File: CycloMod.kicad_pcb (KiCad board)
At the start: 4 copper layers, 22 x 22 mm, 72 parts, among them J1 MICROMOD-2222, U1 10CL010YM164, U2 W25Q128JVS, U3 1.2V, U4 RP2350_60QFN, U5 MIC5504-2.5YMT, Y1 ABM8-272-T3

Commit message: all connected, cleaning up
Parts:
- C23: moved to B.Cu
- R5, R7: moved to F.Cu
- moved C3 10.6 mm to (149.1, 99.4), turned to 0 degrees
- moved C23 10.4 mm to (157.4, 108.1), turned to -90 degrees
- moved R7 7.80 mm to (149.9, 98.8), turned to -90 degrees
- moved R5 7.35 mm to (148.7, 98.3), turned to 0 degrees
- moved C22 4.32 mm to (158.7, 104.0)
- moved C25 2.55 mm to (152.8, 100.4), turned to 0 degrees
- moved C24 1.41 mm to (153.9, 106.7), turned to 0 degrees
- moved D1 1.00 mm to (142.5, 95.8)
- moved D2 1.00 mm to (145.0, 95.7)
- moved D3 1.00 mm to (147.5, 95.7)
- moved R10 1.00 mm to (143.8, 95.2)
- moved R11 1.00 mm to (146.2, 96.2)
- moved R14 1.00 mm to (146.2, 95.2)
- moved R9 1.00 mm to (143.8, 96.2)
- moved U2 1.00 mm to (145.0, 97.5)
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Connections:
- J1 pad GND: (no net) -> GND
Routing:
- net /~{BOOT}: track 39.2 -> 28.6 mm, vias 1 -> 2
- net +3V3: track 54.4 -> 49.3 mm, vias 20 -> 21
- net /QSPI_SS: track 12.8 -> 10.8 mm
- net /G11: track 17.5 -> 15.6 mm
- net /QSPI_SD2: track 16.0 -> 17.7 mm
- net +2V5: track 34.5 -> 33.3 mm
- net Net-(U1E-VCCD_PLL1): track 29.8 -> 29.2 mm
- net GND: track 71.8 -> 71.7 mm, vias 45 -> 51
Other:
- board text added: "CycloMod"

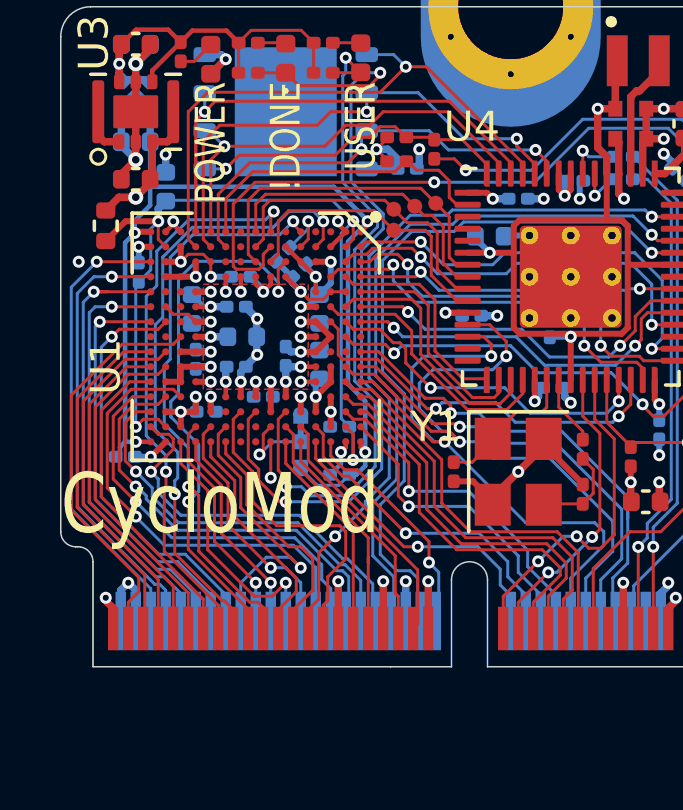
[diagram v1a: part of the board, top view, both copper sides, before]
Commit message: cleaning up nets
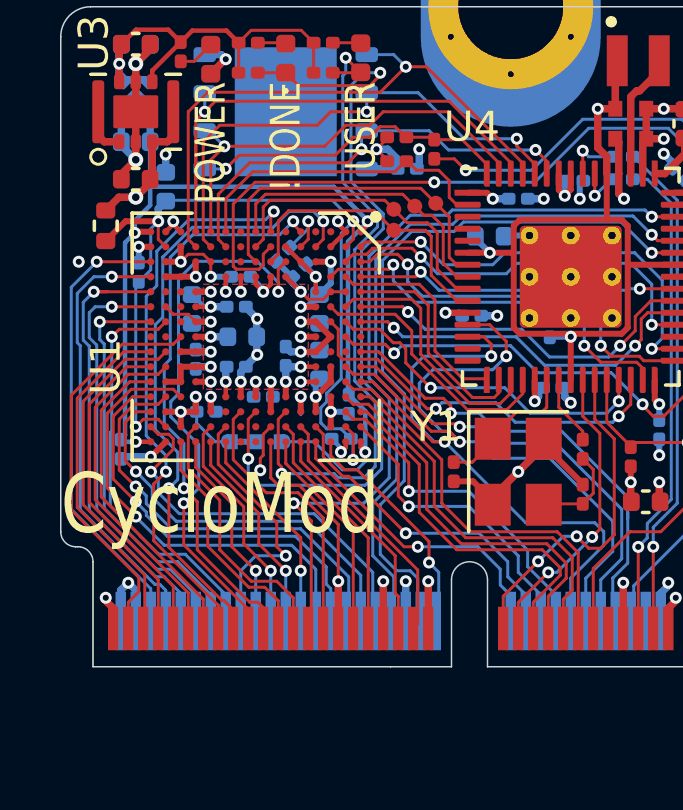
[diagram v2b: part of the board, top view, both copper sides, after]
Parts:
- moved C14 2.37 mm to (147.1, 107.2), turned to -90 degrees
- moved JP2 1.50 mm to (144.0, 108.5), turned to 0 degrees
- moved C30 0.40 mm to (146.8, 108.4)
- moved C15 0.29 mm to (139.5, 108.8), turned to -90 degrees
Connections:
- U1 pad K15: /SDA1 -> /AUD_BCLK
- U1 pad L14: /AUD_BCLK -> /AUD_IN
- U1 pad L15: /SCL1 -> /AUD_LRCLK
- U1 pad M14: /AUD_OUT -> /SDA1
- U1 pad M15: /AUD_IN -> /AUD_OUT
- U1 pad N15: /AUD_LRCLK -> /SCL1
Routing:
- net GND: track 71.7 -> 78.5 mm, vias 51 -> 50
- net /BATT_VIN/3: track 24.7 -> 26.5 mm
- net /AUD_LRCLK: track 8.68 -> 7.01 mm
- net /PWM1: track 10.4 -> 9.19 mm
- net /AUD_BCLK: track 8.22 -> 7.01 mm
- net /MSEL1: track 2.63 -> 1.59 mm
- net /AUD_MCLK: track 9.71 -> 8.72 mm
- net /SDA1: track 7.93 -> 8.78 mm
- net Net-(U1E-VCCD_PLL1): track 29.2 -> 30.0 mm
- net /AUD_OUT: track 7.54 -> 6.80 mm
- net /INIT: track 22.6 -> 21.9 mm
- net /AUD_IN: track 7.01 -> 7.51 mm
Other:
- board text added: "AS|JTAG"
- board text removed: "JT AS"

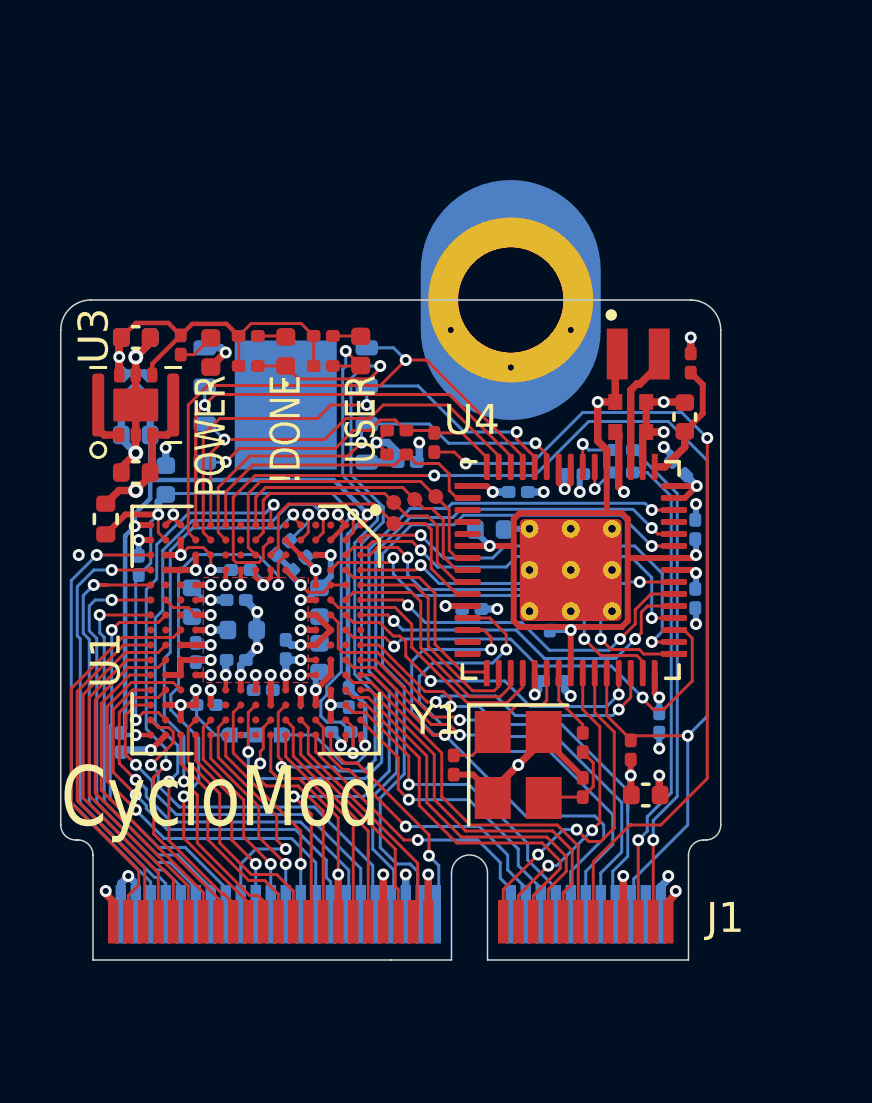
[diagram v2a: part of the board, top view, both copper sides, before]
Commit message: cleaned up some DRC, modified mechanical mounting half hole
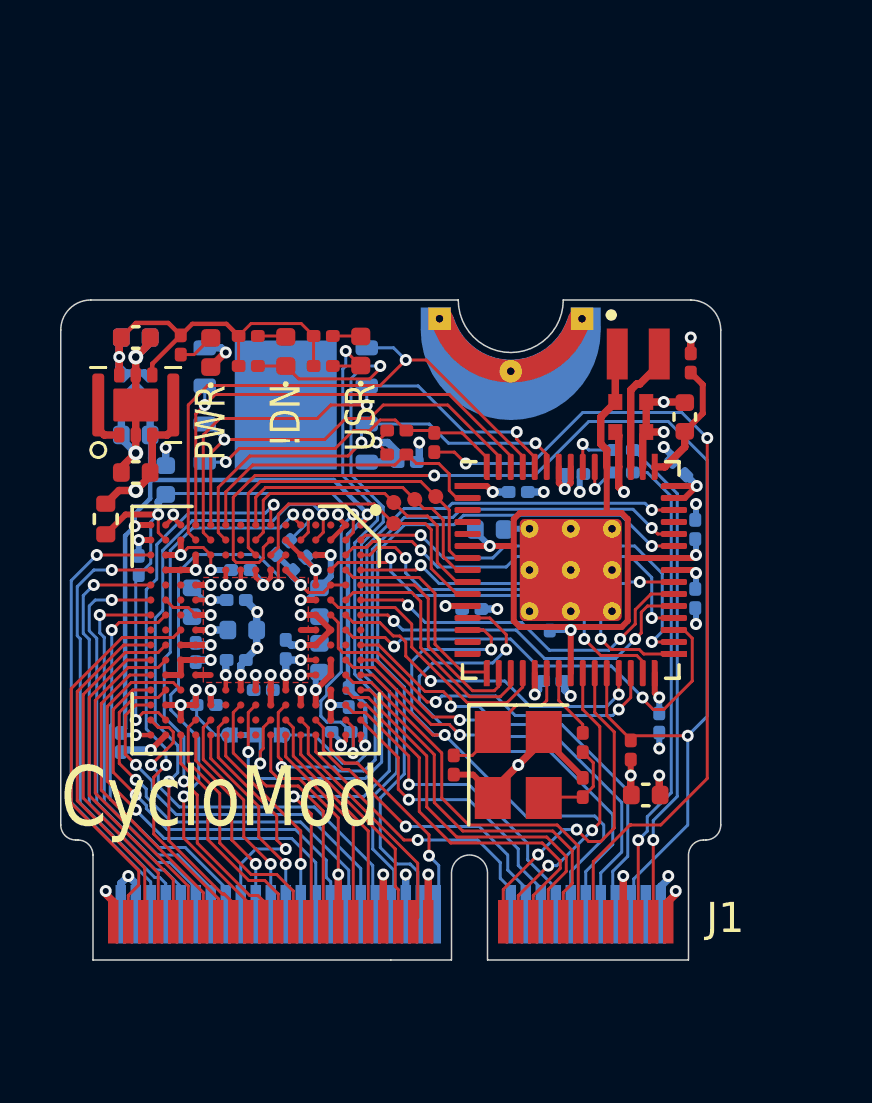
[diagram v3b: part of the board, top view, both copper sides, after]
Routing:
- net /QSPI_SD2: track 17.7 -> 16.3 mm
- net /MSEL1: track 1.59 -> 2.61 mm
- net GND: track 78.5 -> 77.9 mm, vias 50 -> 46
- net +1V1: track 28.2 -> 27.7 mm, vias 4 -> 3
- net +1V2: vias 12 -> 10
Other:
- outline, holes or cut-outs redrawn
- board text added: "!DN"
- board text added: "PWR"
- board text added: "USR"
- board text removed: "!DONE"
- board text removed: "POWER"
- board text removed: "USER"

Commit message: fixed QMI SD1 pull-down, cleaned up notes
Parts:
- removed FRAME1: FRAME-LEDGER, MicroMod-RP2040-ProcessorBoard:CREATIVE_COMMONS
- added R15: 10k, Resistor_SMD:R_0201_0603Metric, F.Cu at (149.4, 97.5)
- U2: value W25Q128JVS -> W25Q128JVP
- moved LOGO4 45.5 mm to (150.0, 25.0)
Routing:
- net +1V2: track 24.5 -> 23.3 mm
- net GND: track 77.9 -> 78.5 mm, vias 46 -> 47
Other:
- board text added: "0.8mm PCB Four layer design 45 degree chamfered edge Hard gold plating on card edge (min 15 micro inches)"
- board text added: "Released under the Creative Commons Attribution Share-Alike 4.0 License https://creativecommons.org/licenses/by-sa/4.0/ Derived from MicroMod RP2040 Processor Board by: N. Seidle, SparkFun"
- board text removed: "0.8mm PCB 45 degree chamfered edge Four layer design"
- board text removed: "N. Seidle"

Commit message: fixed BOM and re-sync to pcb
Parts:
- removed LOGO4: SPECIAL_INSTRUCTIONS-ORDERING, MicroMod-RP2040-ProcessorBoard:ORDERING_INSTRUCTIONS
- added FRAME1: FRAME-LEDGER, MicroMod-RP2040-ProcessorBoard:CREATIVE_COMMONS, F.Cu at (159.4, 156.6)
- U1: value 10CL010YM164 -> 10CL016YM164
- U5: value MIC5504-2.5YMT -> XC6223-2.5V
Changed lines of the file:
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@@
 	(layers
 		(0 "F.Cu" signal)
-		(4 "In1.Cu" signal)
-		(6 "In2.Cu" signal)
+		(4 "In1.Cu" power)
+		(6 "In2.Cu" power)
 		(2 "B.Cu" signal)
 		(9 "F.Adhes" user "F.Adhesive")
@@
 	)
 	(setup
+		(stackup
+			(layer "F.SilkS"
+				(type "Top Silk Screen")
+			)
+			(layer "F.Paste"
+				(type "Top Solder Paste")
+			)
+			(layer "F.Mask"
+				(type "Top Solder Mask")
+				(thickness 0.01)
+			)
+			(layer "F.Cu"
+				(type "copper")
+				(thickness 0.035)
+			)
+			(layer "dielectric 1"
+				(type "core")
+				(thickness 0.48)
+				(material "FR4")
+				(epsilon_r 4.5)
+				(loss_tangent 0.02)
+			)
+			(layer "In1.Cu"
+				(type "copper")
+				(thickness 0.035)
+			)
+			(layer "dielectric 2"
+				(type "prepreg")
+				(thickness 0.48)
+				(material "FR4")
+				(epsilon_r 4.5)
+				(loss_tangent 0.02)
+			)
+			(layer "In2.Cu"
+				(type "copper")
+				(thickness 0.035)
+			)
+			(layer "dielectric 3"
+				(type "core")
+				(thickness 0.48)
+				(material "FR4")
+				(epsilon_r 4.5)
+				(loss_tangent 0.02)
+			)
+			(layer "B.Cu"
+				(type "copper")
+				(thickness 0.035)
+			)
+			(layer "B.Mask"
+				(type "Bottom Solder Mask")
+				(thickness 0.01)
+			)
+			(layer "B.Paste"
+				(type "Bottom Solder Paste")
+			)
+			(layer "B.SilkS"
+				(type "Bottom Silk Screen")
+			)
+			(copper_finish "ENIG")
+			(dielectric_constraints no)
+			(edge_connector bevelled)
+		)
 		(pad_to_mask_clearance 0)
 		(allow_soldermask_bridges_in_footprints no)
@@
 			)
 		)
-		(property "Value" "10CL010YM164"
+		(property "Value" "10CL016YM164"
 			(at 0 4.5 90)
 			(layer "F.Fab")
@@
 			)
 		)
-		(property "LCSC" "C1550733"
+		(property "LCSC" "C6063581"
 			(at 0 0 270)
 			(unlocked yes)
@@
 			)
 		)
-		(property "MPN" "10CL010YM164I7G"
+		(property "MPN" "10CL016YM164I7G"
 			(at 0 0 270)
 			(unlocked yes)
@@
 		)
 	)
-	(footprint "MicroMod-RP2040-ProcessorBoard:ORDERING_INSTRUCTIONS"
-		(layer "F.Cu")
-		(at 150 25)
-		(descr "<h3>Special Ordering Instructions Alert</h3>\n<p>Indicates that the PCB material, colors, copper weights, and/or thickness are non-standard.</p>\n<p>(Standard is 1.6mm FR4, 1 oz copper, immersion silver plating, red soldermask, white silkscreen.)</p>\n<p>Use 0.7\" Vector font @ 8% ratio")
-		(property "Reference" "LOGO4"
-			(at 0 -3.84 0)
-			(layer "F.SilkS")
-			(hide yes)
-			(effects
-				(font
-					(size 1.27 1.27)
-					(thickness 0.15)
-				)
-			)
-		)
-		(property "Value" "SPECIAL_INSTRUCTIONS-ORDERING"
-			(at 24.905 -2.57 0)
-			(layer "F.Fab")
-			(hide yes)
-			(effects
-				(font
-					(size 1.27 1.27)
-					(thickness 0.15)
-				)
-			)
-		)
-		(property "Datasheet" ""
-			(at 0 0 0)
-			(layer "F.Fab")
-			(hide yes)
-			(effects
-				(font
-					(size 1.27 1.27)
-					(thickness 0.15)
-				)
-			)
-		)
-		(property "Description" ""
-			(at 0 0 0)
-			(layer "F.Fab")
-			(hide yes)
-			(effects
-				(font
-					(size 1.27 1.27)
-					(thickness 0.15)
-				)
-			)
-		)
-		(property "LCSC" ""
-			(at 0 0 0)
-			(unlocked yes)
-			(layer "F.Fab")
-			(hide yes)
-			(effects
-				(font
-					(size 1 1)
-					(thickness 0.15)
-				)
-			)
-		)
-		(property "MPN" ""
-			(at 0 0 0)
-			(unlocked yes)
-			(layer "F.Fab")
-			(hide yes)
-			(effects
-				(font
-					(size 1 1)
-					(thickness 0.15)
-				)
-			)
-		)
-		(sheetname "/")
-		(sheetfile "CycloMod.kicad_sch")
-		(attr exclude_from_bom)
-		(fp_line
-			(start 0 0)
-			(end 101.6 0)
-			(stroke
-				(width 0.2032)
-				(type solid)
-			)
-			(layer "F.Fab")
-		)
-		(fp_line
-			(start 0 8.89)
-			(end 0 0)
-			(stroke
-				(width 0.2032)
-				(type solid)
-			)
-			(layer "F.Fab")
-		)
-		(fp_line
-			(start 0 8.89)
-			(end 101.6 8.89)
-			(stroke
-				(width 0.2032)
-				(type solid)
-			)
-			(layer "F.Fab")
-		)
-		(fp_line
-			(start 0 50.8)
-			(end 0 8.89)
-			(stroke
-				(width 0.2032)
-				(type solid)
-			)
-			(layer "F.Fab")
-		)
-		(fp_line
-			(start 101.6 0)
-			(end 101.6 8.89)
-			(stroke
-				(width 0.2032)
-				(type solid)
-			)
-			(layer "F.Fab")
-		)
-		(fp_line
-			(start 101.6 8.89)
-			(end 101.6 50.8)
-			(stroke
-				(width 0.2032)
-				(type solid)
-			)
-			(layer "F.Fab")
-		)
-		(fp_line
-			(start 101.6 50.8)
-			(end 0 50.8)
-			(stroke
-				(width 0.2032)
-				(type solid)
-			)
-			(layer "F.Fab")
-		)
-		(fp_text user "Ordering Instructions:"
-			(at 1.27 1.27 0)
-			(layer "F.Fab")
-			(effects
-				(font
-					(size 2.5908 2.5908)
-					(thickness 0.4572)
-				)
-				(justify left top)
-			)
-		)
-		(fp_text user "(Add these comments when uploading gerbers.)"
-			(at 1.27 6.35 0)
-			(layer "F.Fab")
-			(effects
-				(font
-					(size 1.63576 1.63576)
-					(thickness 0.14224)
-				)
-				(justify left top)
-			)
-		)
-		(embedded_fonts no)
-	)
 	(footprint "LED_SMD:LED_0402_1005Metric"
 		(layer "F.Cu")
@@
 		)
 	)
+	(footprint "MicroMod-RP2040-ProcessorBoard:CREATIVE_COMMONS"
+		(layer "F.Cu")
+		(at 159.385 156.591)
+		(descr "<h3>Creative Commons License Template</h3>\n<p>CC BY-SA 4.0 License with <a href=\"https://creativecommons.org/licenses/by-sa/4.0/\">link to license</a> and placeholder for designer name.</p>\n<p>Devices using:\n<ul><li>FRAME_LEDGER</li>\n<li>FRAME_LETTER</li></ul></p>")
+		(property "Reference" "FRAME1"
+			(at 0 0 0)
+			(layer "F.SilkS")
+			(hide yes)
+			(effects
+				(font
+					(size 1.27 1.27)
+					(thickness 0.15)
+				)
+			)
+		)
+		(property "Value" "FRAME-LEDGER"
+			(at 0 0 0)
+			(layer "F.Fab")
+			(hide yes)
+			(effects
+				(font
+					(size 1.27 1.27)
+					(thickness 0.15)
+				)
+			)
+		)
+		(property "Datasheet" ""
+			(at 0 0 0)
+			(layer "F.Fab")
+			(hide yes)
+			(effects
+				(font
+					(size 1.27 1.27)
+					(thickness 0.15)
+				)
+			)
+		)
+		(property "Description" ""
+			(at 0 0 0)
+			(layer "F.Fab")
+			(hide yes)
+			(effects
+				(font
+					(size 1.27 1.27)
+					(thickness 0.15)
+				)
+			)
+		)
+		(property "LCSC" ""
+			(at 0 0 0)
+			(unlocked yes)
+			(layer "F.Fab")
+			(hide yes)
+			(effects
+				(font
+					(size 1 1)
+					(thickness 0.15)
+				)
+			)
+		)
+		(property "MPN" ""
+			(at 0 0 0)
+			(unlocked yes)
+			(layer "F.Fab")
+			(hide yes)
+			(effects
+				(font
+					(size 1 1)
+					(thickness 0.15)
+				)
+			)
+		)
+		(sheetname "/")
+		(sheetfile "CycloMod.kicad_sch")
+		(attr exclude_from_bom)
+		(embedded_fonts no)
+	)
 	(footprint "custom:C_0402_1005Metric_small_pads"
 		(layer "F.Cu")
@@
 			)
 		)
-		(property "Value" "MIC5504-2.5YMT"
+		(property "Value" "XC6223-2.5V"
 			(at 0 -2 90)
 			(layer "B.Fab")
